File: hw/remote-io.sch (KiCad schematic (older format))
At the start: 1 part, among them P1 CONN_02X20

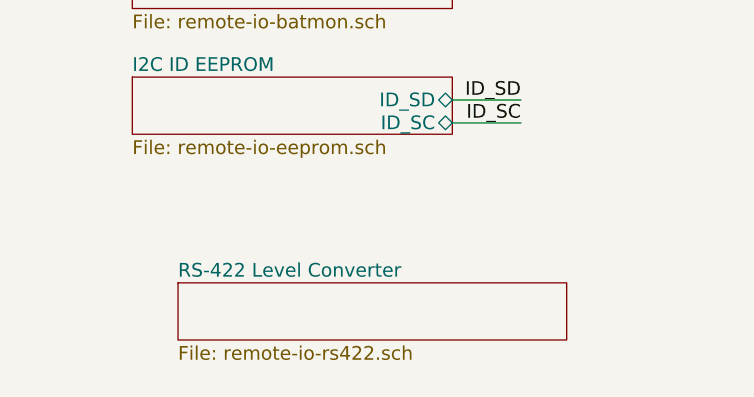
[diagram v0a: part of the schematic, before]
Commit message: Added RS-422 Receiver Circuit
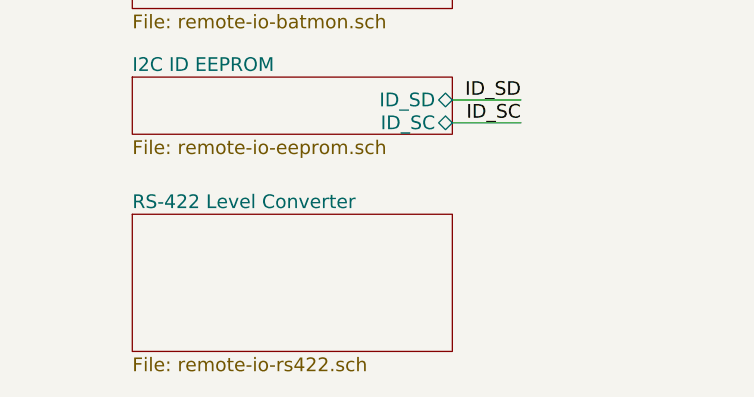
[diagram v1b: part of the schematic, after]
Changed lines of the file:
@@
 $Descr USLetter 11000 8500
 encoding utf-8
-Sheet 1 4
+Sheet 1 5
 Title "Remote I/O Top Level"
 Date "2015-06-15"
@@
 	8000 2750 8600 2750
 $Sheet
-S 4300 4950 1700 250
+S 4100 4650 1400 600
 U 55823A24
 F0 "RS-422 Level Converter" 60

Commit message: RS-422 Tweaks
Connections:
- net labels added: RS422_GPS, RXD0
- wire segments 28 -> 32
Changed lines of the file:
@@
 $EndDescr
 $Sheet
-S 4100 2450 1400 150
+S 4100 2400 1400 150
 U 557F39A6
 F0 "Power" 60
@@
 ID_SC
 $Sheet
-S 4100 4050 1400 250
+S 4100 4050 1400 300
 U 55817EDD
 F0 "I2C ID EEPROM" 60
@@
 	8000 2750 8600 2750
 $Sheet
-S 4100 4650 1400 600
+S 4100 4650 1400 350
 U 55823A24
 F0 "RS-422 Level Converter" 60
 F1 "remote-io-rs422.sch" 60
+F2 "~RS422_GPS" I R 5500 4900 60
+F3 "RS422_GPS" I R 5500 4750 60
+F4 "RX_GPS" O L 4100 4750 60
 $EndSheet
+Text Label 3850 4750 0    60   ~ 0
+RXD0
+Wire Wire Line
+	4100 4750 3850 4750
+Text Label 5550 4750 0    60   ~ 0
+RS422_GPS
+Text Label 5550 4900 0    60   ~ 0
+RS422_GPS
+Wire Wire Line
+	5500 4750 6050 4750
+Wire Wire Line
+	5500 4900 6050 4900
+Text Label 8000 2050 0    60   ~ 0
+RXD0
+Wire Wire Line
+	8250 2050 8000 2050
 $EndSCHEMATC

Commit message: Finished first revision of schematic
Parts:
- added D?: LED0, symbol LED
- added D?: LED1, symbol LED
- added D?: LED2, symbol LED
- added D?: LED3, symbol LED
- added P?: CONN_01X02, symbol CONN_01X02
- added P? (x3): CONN_01X08, symbol CONN_01X08
- added P?: CONN_01X04, symbol CONN_01X04
- added R? (x4): 65, symbol R
- added R? (x3): 0, symbol R
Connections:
- net labels added: LED0, LED1, LED2, LED3, SW_IN0, SW_IN1, SW_IN2, SW_IN3, SW_IN4, SW_IN5, SW_IN6, SW_IN7, ~RS422_GPS
- wire segments 32 -> 97
- no-connect marks 0 -> 9
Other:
- note added: "Battery Measurement"
- note added: "GPIO: Indication LEDs and Switch Monitor"
- note added: "Identification and Configuration EEPROM"
- note added: "Power Input, Regulation, and Protection"
- note added: "RS-422 GPS Connector and Level Conversion"
- note added: "Raspberry Pi 2 GPIO Header"
- moved on the sheet: P1

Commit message: Matched all footprints to schem and created kicad_pcb file
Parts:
- removed R? (x3): 0, symbol R
- D1, D2, D3, D4: renamed from D?; footprint (none) -> LEDs:LED-0805
- P1: renamed from P?; footprint (none) -> remote-io:OSTTE020104
- P2, P3, P5: renamed from P?; footprint (none) -> remote-io:OSTTE080104
- P4: renamed from P1; footprint (none) -> Pin_Headers:Pin_Header_Straight_2x20
- P6: renamed from P?; footprint (none) -> remote-io:OSTTE040104
- R2, R4, R6, R7: renamed from R?; footprint (none) -> Resistors_SMD:R_0805_HandSoldering
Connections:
- net labels removed: GNDA, GNDD, GNDPWR
- wire segments 97 -> 82
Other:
- moved on the sheet: P1

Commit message: added CAN power, controller, and transceiver to schem and updated PCB
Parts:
- added P7: CONN_01X02, remote-io:OSTTE020104, symbol CONN_01X02
- renumbered R2 to R1, R4 to R2, R6 to R3, R7 to R4
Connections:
- net labels added: +5VA, CAN_H, CAN_L, CAN_VSENSE, CAN_~INT, SPI_CE1_N
- wire segments 82 -> 92
- no-connect marks 9 -> 6
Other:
- note added: "CAN Connector, Controller, and Transceiver"
- moved on the sheet: P6

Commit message: Started fucking aroond with pcb layout. Power is tricky...
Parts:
- removed P5: CONN_01X08, remote-io:OSTTE080104, symbol CONN_01X08
- renumbered P7 to P10, P4 to P5, P6 to P8
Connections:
- wire segments 92 -> 84
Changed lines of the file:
@@
 F4 "ADC_DIN" I L 1650 5600 60
 F5 "ADC_DOUT" O L 1650 5700 60
-F6 "BAT_MEAS4" I R 3050 5600 60
-F7 "BAT_MEAS5" I R 3050 5700 60
-F8 "BAT_MEAS6" I R 3050 5800 60
-F9 "BAT_MEAS7" I R 3050 5900 60
 F10 "BAT_MEAS0" I R 3050 5200 60
 F11 "BAT_MEAS1" I R 3050 5300 60
@@
 $EndComp
 $Comp
-L CONN_02X20 P4
+L CONN_02X20 P5
 U 1 1 557F7DEF
 P 9000 3550
-F 0 "P4" H 9000 4600 50  0000 C CNN
+F 0 "P5" H 9000 4600 50  0000 C CNN
 F 1 "CONN_02X20" V 9000 3550 50  0000 C CNN
 F 2 "Pin_Headers:Pin_Header_Straight_2x20" H 9000 2600 60  0001 C CNN
@@
 	-1   0    0    -1
 $EndComp
-$Comp
-L CONN_01X08 P3
-U 1 1 5581251E
-P 2800 3400
-F 0 "P3" H 2800 3850 50  0000 C CNN
-F 1 "CONN_01X08" V 2900 3400 50  0000 C CNN
-F 2 "remote-io:OSTTE080104" H 2800 3400 60  0001 C CNN
-F 3 "" H 2800 3400 60  0000 C CNN
-	1    2800 3400
-	1    0    0    -1
-$EndComp
 Text Label 2050 3250 0    60   ~ 0
 BAT_MEAS1
@@
 Text Label 3100 5600 0    60   ~ 0
 BAT_MEAS4
-$Comp
-L CONN_01X08 P5
-U 1 1 558175A9
-P 2800 4350
-F 0 "P5" H 2800 4800 50  0000 C CNN
-F 1 "CONN_01X08" V 2900 4350 50  0000 C CNN
-F 2 "remote-io:OSTTE080104" H 2800 4350 60  0001 C CNN
-F 3 "" H 2800 4350 60  0000 C CNN
-	1    2800 4350
-	1    0    0    -1
-$EndComp
-Text Label 2050 4000 0    60   ~ 0
-BAT_MEAS4
-Text Label 2050 4200 0    60   ~ 0
-BAT_MEAS5
-Text Label 2050 4400 0    60   ~ 0
-BAT_MEAS6
-Text Label 2050 4600 0    60   ~ 0
-BAT_MEAS7
-$Comp
-L CONN_01X08 P2
-U 1 1 5581A2ED
-P 5400 1650
-F 0 "P2" H 5400 2100 50  0000 C CNN
-F 1 "CONN_01X08" V 5500 1650 50  0000 C CNN
-F 2 "remote-io:OSTTE080104" H 5400 1650 60  0001 C CNN
-F 3 "" H 5400 1650 60  0000 C CNN
-	1    5400 1650
-	1    0    0    -1
-$EndComp
 Text Label 4650 1300 0    60   ~ 0
 SW_IN0
@@
 Identification and Configuration EEPROM
 $Comp
-L CONN_01X04 P6
+L CONN_01X04 P8
 U 1 1 558384E2
 P 7200 4500
-F 0 "P6" H 7200 4750 50  0000 C CNN
+F 0 "P8" H 7200 4750 50  0000 C CNN
 F 1 "CONN_01X04" V 7300 4500 50  0000 C CNN
 F 2 "remote-io:OSTTE040104" H 7200 4500 60  0001 C CNN
@@
 L GND #PWR025
 U 1 1 5582D76A
-P 1850 4700
-F 0 "#PWR025" H 1850 4450 50  0001 C CNN
-F 1 "GND" H 1850 4550 50  0000 C CNN
-F 2 "" H 1850 4700 60  0000 C CNN
-F 3 "" H 1850 4700 60  0000 C CNN
-	1    1850 4700
+P 1850 3850
+F 0 "#PWR025" H 1850 3600 50  0001 C CNN
+F 1 "GND" H 1850 3700 50  0000 C CNN
+F 2 "" H 1850 3850 60  0000 C CNN
+F 3 "" H 1850 3850 60  0000 C CNN
+	1    1850 3850
 	-1   0    0    -1
 $EndComp
@@
 CAN_L
 $Comp
-L CONN_01X02 P7
+L CONN_01X02 P10
 U 1 1 5583C21E
 P 7600 5950
-F 0 "P7" H 7600 6100 50  0000 C CNN
+F 0 "P10" H 7600 6100 50  0000 C CNN
 F 1 "CONN_01X02" V 7700 5950 50  0000 C CNN
 F 2 "remote-io:OSTTE020104" H 7600 5950 60  0001 C CNN
@@
 	3050 5600 3600 5600
 Wire Wire Line
-	2600 4000 2050 4000
-Wire Wire Line
-	2600 4200 2050 4200
-Wire Wire Line
-	2600 4400 2050 4400
-Wire Wire Line
-	2600 4600 2050 4600
-Wire Wire Line
-	1850 4700 2600 4700
-Wire Wire Line
-	1850 4500 2600 4500
-Wire Wire Line
-	1850 4300 2600 4300
-Wire Wire Line
-	1850 4100 2600 4100
-Wire Wire Line
 	5200 1300 4650 1300
 Wire Wire Line
@@
 	10000 2350 8050 2350
 Wire Wire Line
-	1850 3150 1850 4700
+	1850 3150 1850 3850
 Connection ~ 1850 3350
 Connection ~ 1850 3550
 Connection ~ 1850 3750
-Connection ~ 1850 4100
-Connection ~ 1850 4300
-Connection ~ 1850 4500
 Wire Notes Line
 	1250 1000 1250 2050
@@
 Wire Wire Line
 	6800 5800 7400 5800
+$Comp
+L CONN_01X08 P3
+U 1 1 55841FAA
+P 2800 3400
+F 0 "P3" H 2800 3850 50  0000 C CNN
+F 1 "CONN_01X08" V 2900 3400 50  0000 C CNN
+F 2 "remote-io:OSTTE080104" H 2800 3400 60  0001 C CNN
+F 3 "" H 2800 3400 60  0000 C CNN
+	1    2800 3400
+	1    0    0    -1
+$EndComp
+$Comp
+L CONN_01X08 P2
+U 1 1 55842450
+P 5400 1650
+F 0 "P2" H 5400 2100 50  0000 C CNN
+F 1 "CONN_01X08" V 5500 1650 50  0000 C CNN
+F 2 "remote-io:OSTTE080104" H 5400 1650 60  0001 C CNN
+F 3 "" H 5400 1650 60  0000 C CNN
+	1    5400 1650
+	1    0    0    -1
+$EndComp
+Connection ~ 7000 4650
+Connection ~ 7000 4350
+Connection ~ 8300 2600
+Connection ~ 8350 3000
+Connection ~ 8350 3400
+Connection ~ 8350 3800
+Connection ~ 8350 4500
+Connection ~ 9600 4000
+Connection ~ 9600 4200
+Connection ~ 9850 3500
+Connection ~ 9850 3200
+Connection ~ 9600 2600
+Connection ~ 9600 2800
+Connection ~ 1400 1400
+Connection ~ 1400 1300
+Connection ~ 2050 1300
+Connection ~ 2450 1300
+Connection ~ 2850 1300
+Connection ~ 3250 1300
+Connection ~ 3600 1350
 $EndSCHEMATC

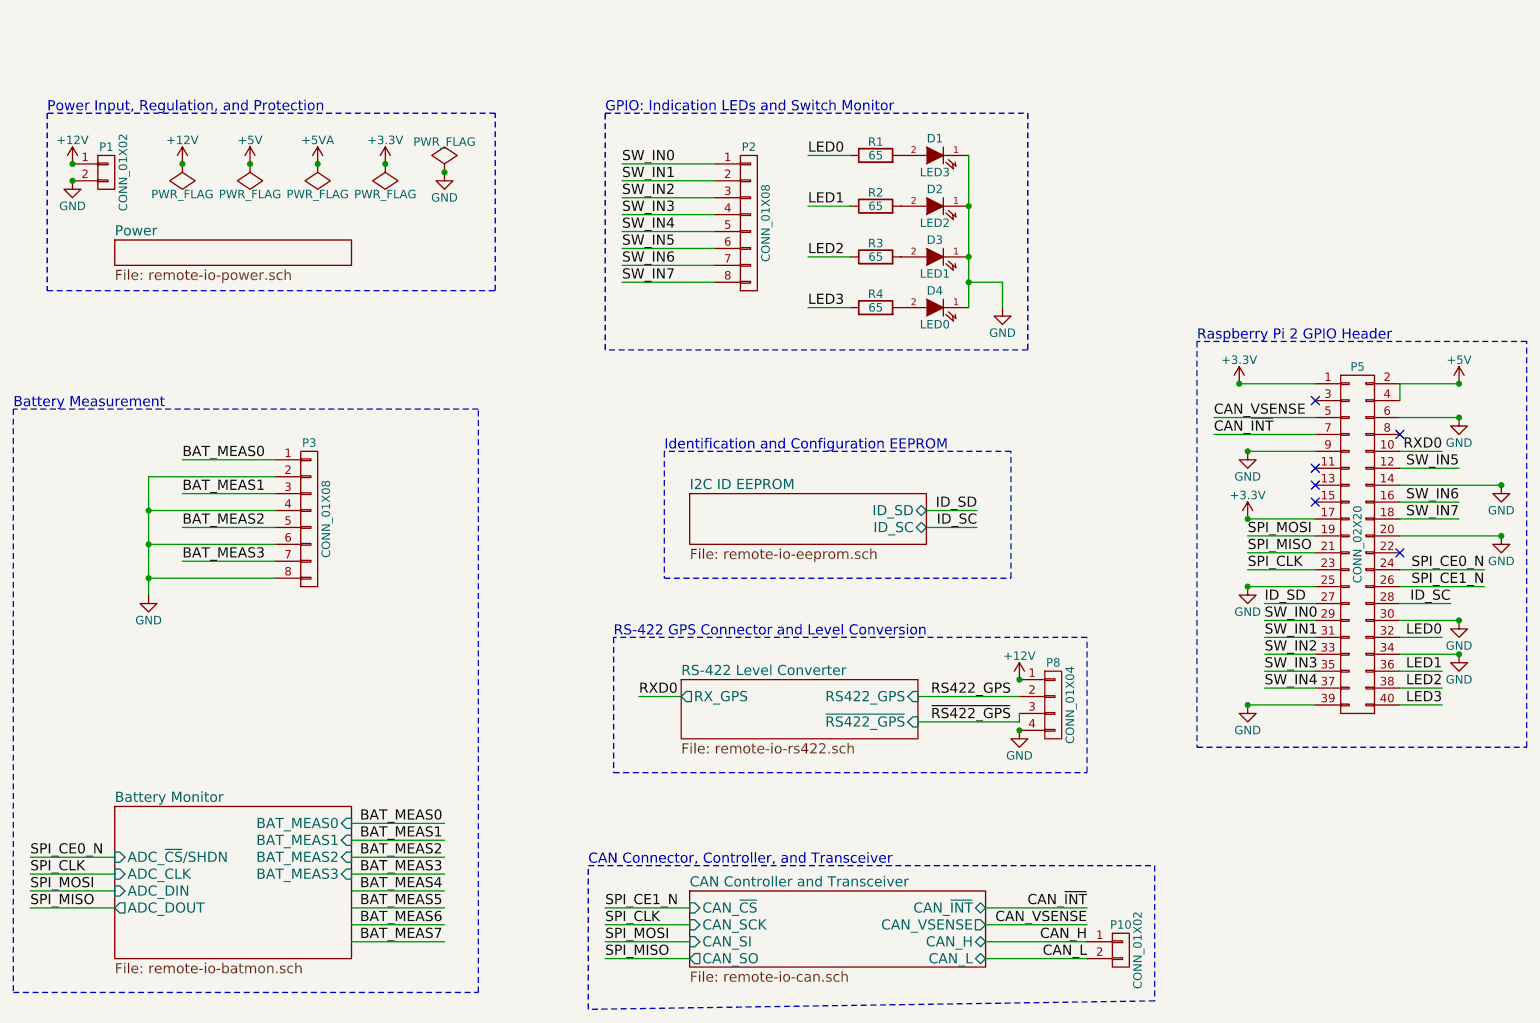
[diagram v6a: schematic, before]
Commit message: All parts in hat-spec-size board
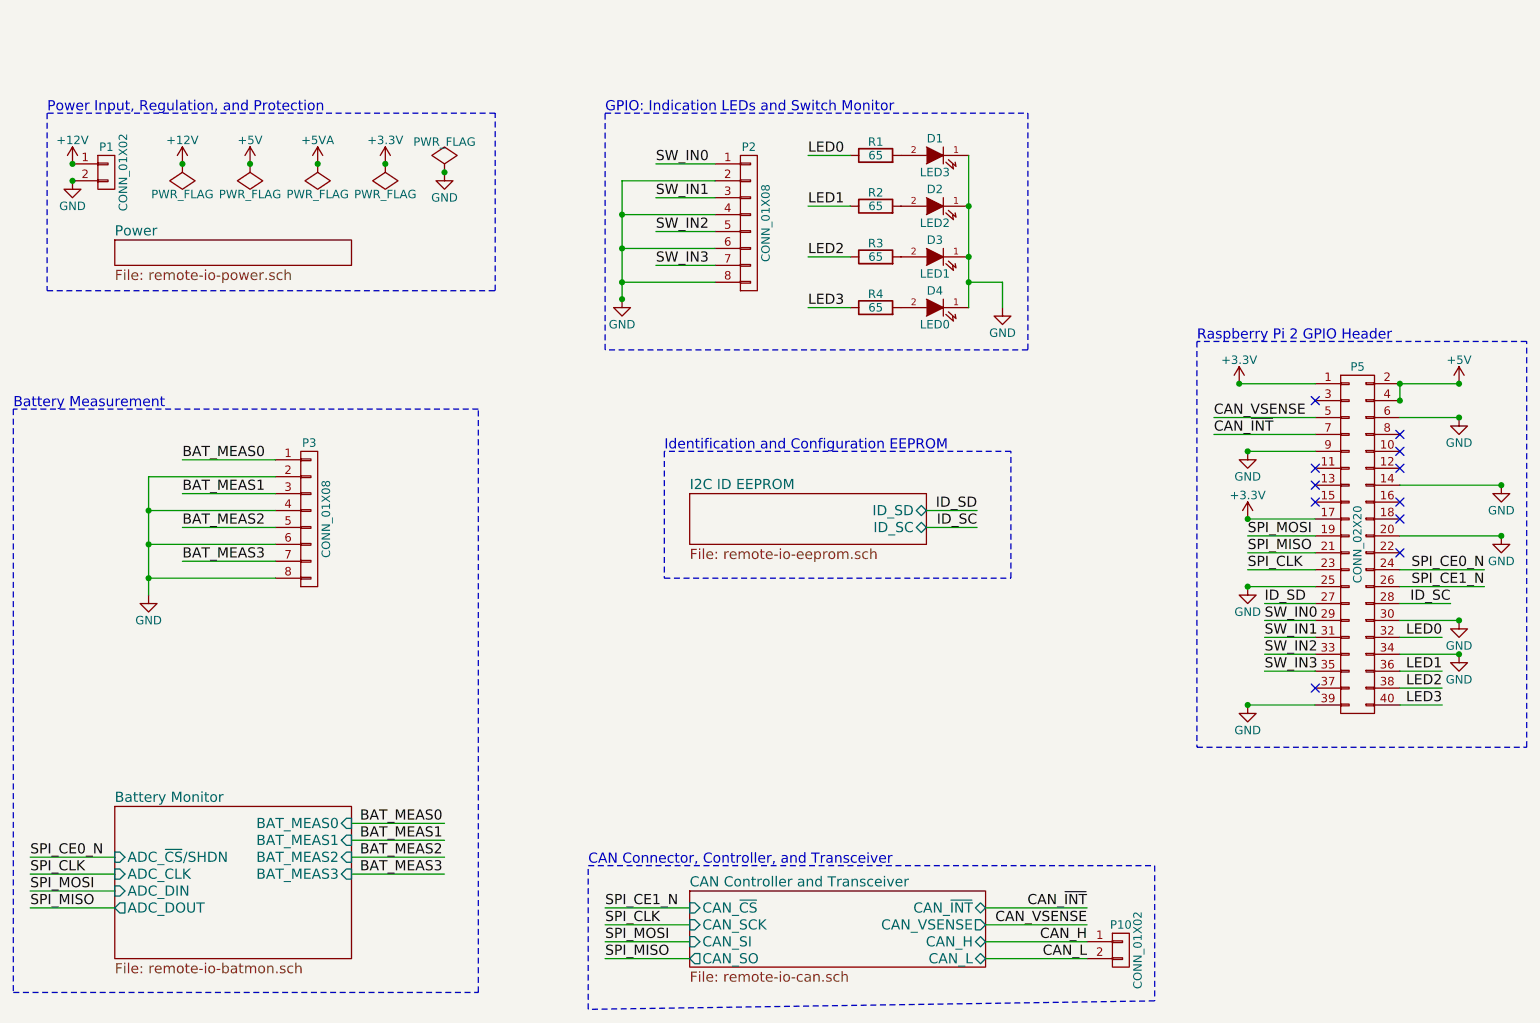
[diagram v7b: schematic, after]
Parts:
- removed P8: CONN_01X04, remote-io:OSTTE040104, symbol CONN_01X04
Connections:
- net labels removed: BAT_MEAS4, BAT_MEAS5, BAT_MEAS6, BAT_MEAS7, RS422_GPS, RXD0, SW_IN4, SW_IN5, SW_IN6, SW_IN7, ~RS422_GPS
- wire segments 84 -> 72
- no-connect marks 6 -> 11
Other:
- note removed: "RS-422 GPS Connector and Level Conversion"
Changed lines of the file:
@@
 $Descr USLetter 11000 8500
 encoding utf-8
-Sheet 1 6
+Sheet 1 5
 Title "Remote I/O Top Level"
 Date "2015-06-15"
@@
 F4 "ADC_DIN" I L 1650 5600 60
 F5 "ADC_DOUT" O L 1650 5700 60
-F10 "BAT_MEAS0" I R 3050 5200 60
-F11 "BAT_MEAS1" I R 3050 5300 60
-F12 "BAT_MEAS2" I R 3050 5400 60
-F13 "BAT_MEAS3" I R 3050 5500 60
+F6 "BAT_MEAS0" I R 3050 5200 60
+F7 "BAT_MEAS1" I R 3050 5300 60
+F8 "BAT_MEAS2" I R 3050 5400 60
+F9 "BAT_MEAS3" I R 3050 5500 60
 $EndSheet
 $Comp
@@
 Text Label 9750 3700 2    60   ~ 0
 SPI_CE0_N
-Text Label 4750 4450 0    60   ~ 0
-RXD0
-Text Label 6950 4450 2    60   ~ 0
-RS422_GPS
-Text Label 6950 4600 2    60   ~ 0
-~RS422_GPS
-Text Label 9500 3000 2    60   ~ 0
-RXD0
 Text Label 9500 4100 2    60   ~ 0
 LED0
@@
 Text Label 2050 3050 0    60   ~ 0
 BAT_MEAS0
-Text Label 3100 5900 0    60   ~ 0
-BAT_MEAS7
-Text Label 3100 5800 0    60   ~ 0
-BAT_MEAS6
-Text Label 3100 5700 0    60   ~ 0
-BAT_MEAS5
-Text Label 3100 5600 0    60   ~ 0
-BAT_MEAS4
-Text Label 4650 1300 0    60   ~ 0
+Text Label 4850 1300 0    60   ~ 0
 SW_IN0
-Text Label 4650 1400 0    60   ~ 0
+Text Label 4850 1500 0    60   ~ 0
 SW_IN1
-Text Label 4650 1500 0    60   ~ 0
+Text Label 4850 1700 0    60   ~ 0
 SW_IN2
-Text Label 4650 1600 0    60   ~ 0
+Text Label 4850 1900 0    60   ~ 0
 SW_IN3
-Text Label 4650 1700 0    60   ~ 0
-SW_IN4
-Text Label 4650 1800 0    60   ~ 0
-SW_IN5
-Text Label 4650 1900 0    60   ~ 0
-SW_IN6
-Text Label 4650 2000 0    60   ~ 0
-SW_IN7
 Text Notes 4550 1000 0    60   ~ 0
 GPIO: Indication LEDs and Switch Monitor
@@
 Text Label 8450 4300 0    60   ~ 0
 SW_IN3
-Text Label 8450 4400 0    60   ~ 0
-SW_IN4
 $Comp
 L GND #PWR012
@@
 	1    0    0    -1
 $EndComp
-Text Label 9600 3100 2    60   ~ 0
-SW_IN5
-Text Label 9600 3300 2    60   ~ 0
-SW_IN6
-Text Label 9600 3400 2    60   ~ 0
-SW_IN7
 NoConn ~ 9250 3600
 NoConn ~ 8750 2700
@@
 Identification and Configuration EEPROM
 $Comp
-L CONN_01X04 P8
-U 1 1 558384E2
-P 7200 4500
-F 0 "P8" H 7200 4750 50  0000 C CNN
-F 1 "CONN_01X04" V 7300 4500 50  0000 C CNN
-F 2 "remote-io:OSTTE040104" H 7200 4500 60  0001 C CNN
-F 3 "" H 7200 4500 60  0000 C CNN
-	1    7200 4500
-	1    0    0    -1
-$EndComp
-Text Notes 4600 4100 0    60   ~ 0
-RS-422 GPS Connector and Level Conversion
-$Comp
 L +5V #PWR015
 U 1 1 5580F5FF
@@
 $EndComp
 $Comp
-L +12V #PWR021
-U 1 1 55811267
-P 7000 4350
-F 0 "#PWR021" H 7000 4200 50  0001 C CNN
-F 1 "+12V" H 7000 4490 50  0000 C CNN
-F 2 "" H 7000 4350 60  0000 C CNN
-F 3 "" H 7000 4350 60  0000 C CNN
-	1    7000 4350
-	1    0    0    -1
-$EndComp
-$Comp
-L PWR_FLAG #FLG022
+L PWR_FLAG #FLG021
 U 1 1 5581068A
 P 3600 1350
-F 0 "#FLG022" H 3600 1445 50  0001 C CNN
+F 0 "#FLG021" H 3600 1445 50  0001 C CNN
 F 1 "PWR_FLAG" H 3600 1530 50  0000 C CNN
 F 2 "" H 3600 1350 60  0000 C CNN
@@
 	1    0    0    -1
 $EndComp
-$Sheet
-S 5000 4350 1400 350
-U 55823A24
-F0 "RS-422 Level Converter" 60
-F1 "remote-io-rs422.sch" 60
-F2 "~RS422_GPS" I R 6400 4600 60
-F3 "RS422_GPS" I R 6400 4450 60
-F4 "RX_GPS" O L 5000 4450 60
-$EndSheet
-$Comp
-L GND #PWR023
-U 1 1 5582A000
-P 7000 4650
-F 0 "#PWR023" H 7000 4400 50  0001 C CNN
-F 1 "GND" H 7000 4500 50  0000 C CNN
-F 2 "" H 7000 4650 60  0000 C CNN
-F 3 "" H 7000 4650 60  0000 C CNN
-	1    7000 4650
-	-1   0    0    -1
-$EndComp
-$Comp
-L GND #PWR024
+$Comp
+L GND #PWR022
 U 1 1 5582B82F
 P 1400 1400
-F 0 "#PWR024" H 1400 1150 50  0001 C CNN
+F 0 "#PWR022" H 1400 1150 50  0001 C CNN
 F 1 "GND" H 1400 1250 50  0000 C CNN
 F 2 "" H 1400 1400 60  0000 C CNN
@@
 $EndComp
 $Comp
-L GND #PWR025
+L GND #PWR023
 U 1 1 5582D76A
 P 1850 3850
-F 0 "#PWR025" H 1850 3600 50  0001 C CNN
+F 0 "#PWR023" H 1850 3600 50  0001 C CNN
 F 1 "GND" H 1850 3700 50  0000 C CNN
 F 2 "" H 1850 3850 60  0000 C CNN
@@
 	9250 3700 9750 3700
 Wire Wire Line
-	5000 4450 4750 4450
-Wire Wire Line
-	6400 4450 7000 4450
-Wire Wire Line
-	6400 4600 7000 4600
-Wire Wire Line
-	9500 3000 9250 3000
-Wire Wire Line
 	9250 4100 9500 4100
 Wire Wire Line
@@
 	2600 3150 1850 3150
 Wire Wire Line
-	3050 5900 3600 5900
-Wire Wire Line
-	3050 5800 3600 5800
-Wire Wire Line
-	3050 5700 3600 5700
-Wire Wire Line
-	3050 5600 3600 5600
-Wire Wire Line
-	5200 1300 4650 1300
-Wire Wire Line
-	5200 1500 4650 1500
-Wire Wire Line
-	5200 1700 4650 1700
-Wire Wire Line
-	5200 1900 4650 1900
-Wire Wire Line
-	5200 2000 4650 2000
-Wire Wire Line
-	5200 1800 4650 1800
+	5200 1300 4850 1300
+Wire Wire Line
+	5200 1700 4850 1700
+Wire Wire Line
+	5200 1400 4650 1400
+Wire Wire Line
+	4650 2000 5200 2000
+Wire Wire Line
+	4650 1800 5200 1800
 Wire Wire Line
 	5200 1600 4650 1600
 Wire Wire Line
-	5200 1400 4650 1400
+	5200 1900 4850 1900
+Wire Wire Line
+	5200 1500 4850 1500
 Wire Notes Line
 	4550 1000 7050 1000
@@
 	8750 4300 8450 4300
 Wire Wire Line
-	8750 4400 8450 4400
-Wire Wire Line
 	8750 4500 8350 4500
 Wire Wire Line
@@
 Wire Wire Line
 	9250 3500 9850 3500
-Wire Wire Line
-	9250 3300 9600 3300
-Wire Wire Line
-	9250 3400 9600 3400
-Wire Wire Line
-	9250 3100 9600 3100
 Wire Notes Line
 	8050 2350 8050 4750
@@
 Wire Notes Line
 	6950 3000 4900 3000
-Wire Notes Line
-	4600 4100 4600 4900
-Wire Notes Line
-	4600 4900 7400 4900
-Wire Notes Line
-	7400 4900 7400 4100
-Wire Notes Line
-	7400 4100 4600 4100
 Wire Wire Line
 	4550 6000 5050 6000
@@
 Wire Wire Line
 	6800 6000 7400 6000
-Wire Wire Line
-	7000 4600 7000 4550
 Wire Notes Line
 	4450 5450 7800 5450
@@
 CAN Connector, Controller, and Transceiver
 $Comp
-L +5VA #PWR026
+L +5VA #PWR024
 U 1 1 5584DE0A
 P 2850 1300
-F 0 "#PWR026" H 2850 1150 50  0001 C CNN
+F 0 "#PWR024" H 2850 1150 50  0001 C CNN
 F 1 "+5VA" H 2850 1440 50  0000 C CNN
 F 2 "" H 2850 1300 60  0000 C CNN
@@
 $EndComp
 $Comp
-L PWR_FLAG #FLG027
+L PWR_FLAG #FLG025
 U 1 1 5584DED9
 P 2850 1300
-F 0 "#FLG027" H 2850 1395 50  0001 C CNN
+F 0 "#FLG025" H 2850 1395 50  0001 C CNN
 F 1 "PWR_FLAG" H 2850 1480 50  0000 C CNN
 F 2 "" H 2850 1300 60  0000 C CNN
@@
 	1    0    0    -1
 $EndComp
-Connection ~ 7000 4650
-Connection ~ 7000 4350
 Connection ~ 8300 2600
 Connection ~ 8350 3000
@@
 Connection ~ 3250 1300
 Connection ~ 3600 1350
+NoConn ~ 9250 3000
+$Comp
+L GND #PWR026
+U 1 1 5589B8EC
+P 4650 2100
+F 0 "#PWR026" H 4650 1850 50  0001 C CNN
+F 1 "GND" H 4650 1950 50  0000 C CNN
+F 2 "" H 4650 2100 60  0000 C CNN
+F 3 "" H 4650 2100 60  0000 C CNN
+	1    4650 2100
+	1    0    0    -1
+$EndComp
+Wire Wire Line
+	4650 1400 4650 2100
+Connection ~ 4650 1600
+Connection ~ 4650 1800
+Connection ~ 4650 2000
+Connection ~ 4650 2100
+NoConn ~ 8750 4400
+NoConn ~ 9250 3300
+NoConn ~ 9250 3400
+Connection ~ 9250 2600
+Connection ~ 9250 2700
+NoConn ~ 9250 3100
 $EndSCHEMATC
